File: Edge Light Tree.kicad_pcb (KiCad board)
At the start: 2 copper layers, 94 x 32 mm, 40 parts, among them M1 Motor_DC, Q1 2SC1815, Q2 2SC1815, Q3 2SC1815, Q4 2SC1815, Q5 2SC1815, Q6 2SC1815, SW1 SW_DIP_x01, SW2 SW_DIP_x01

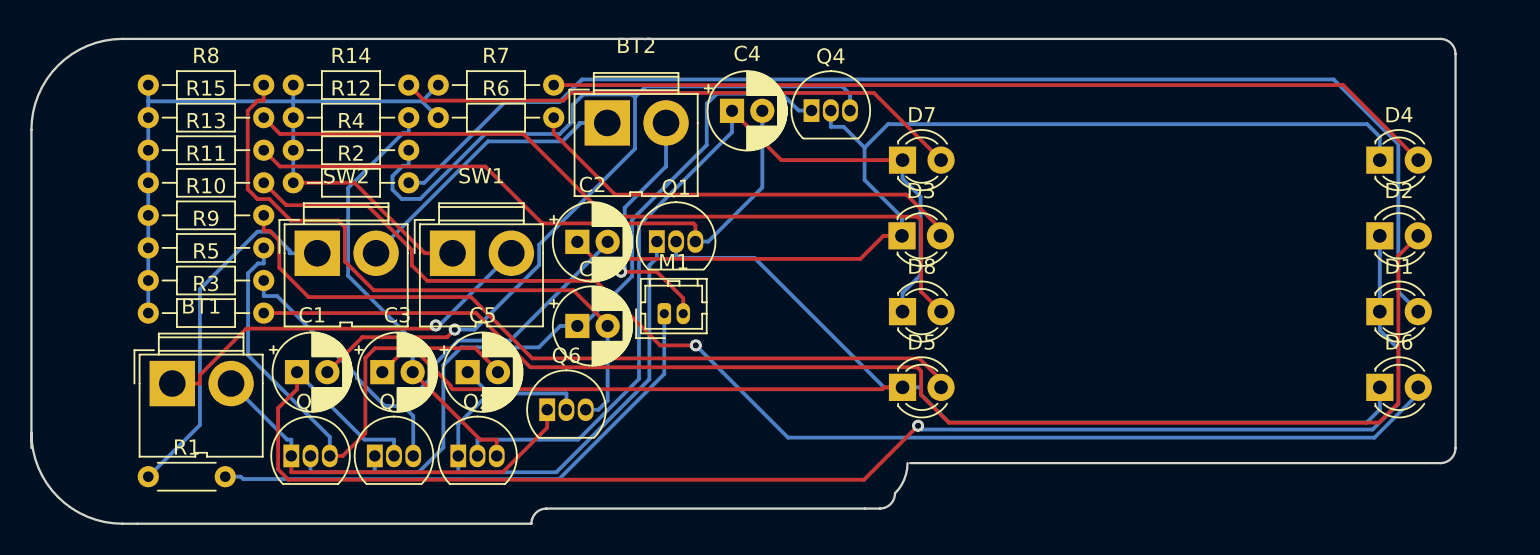
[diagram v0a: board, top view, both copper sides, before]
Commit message: Board mounting holes until installation
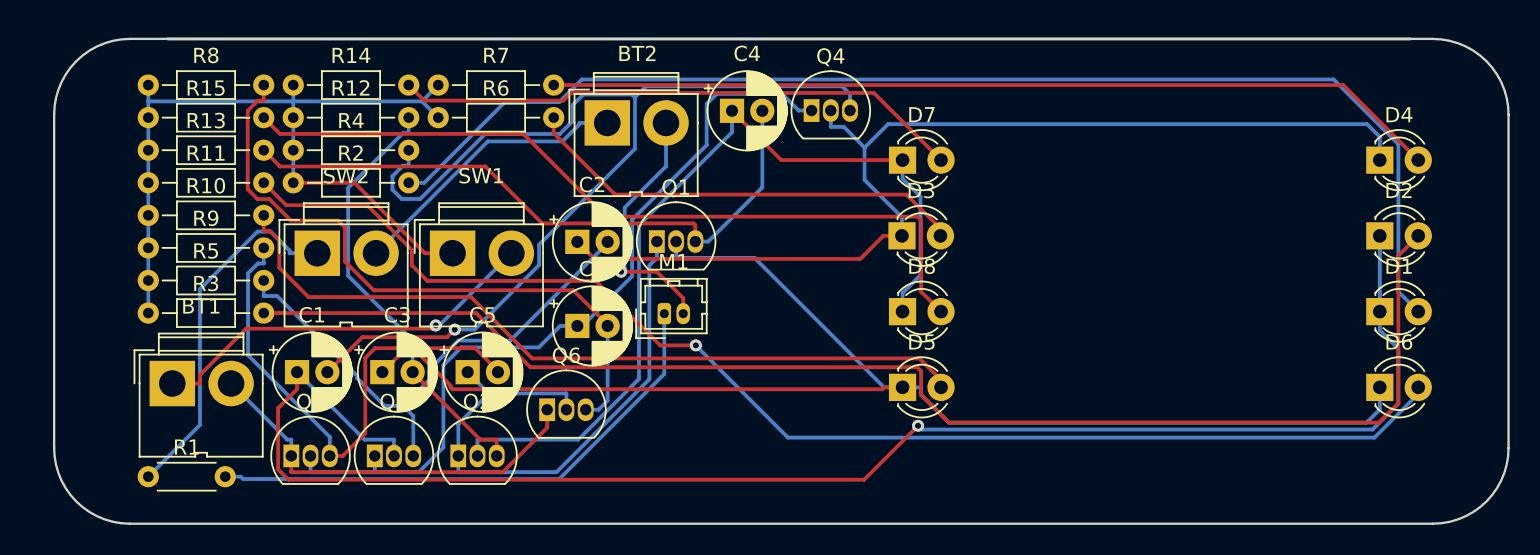
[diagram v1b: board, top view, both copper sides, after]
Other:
- board size 94 x 32 mm -> 96 x 32 mm
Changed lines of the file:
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@@
-(kicad_pcb (version 20171130) (host pcbnew "(5.0.2)-1")
+(kicad_pcb (version 20171130) (host pcbnew "(5.0.1-3-g963ef8bb5)")
   (general
     (thickness 1.6)
-    (drawings 17)
+    (drawings 15)
     (tracks 305)
     (zones 0)
@@
     (descr "JWT A3963, 3.96mm pitch Pin head connector (http://www.jwt.com.tw/pro_pdf/A3963.pdf)")
     (tags "connector JWT A3963 pinhead")
-    (fp_text reference BT2 (at 1.91 -5.08) (layer F.SilkS)
+    (fp_text reference BT2 (at 1.992 -4.5464) (layer F.SilkS)
       (effects (font (size 1 1) (thickness 0.15)))
     )
@@
     )
   )
-  (gr_line (start 110 80) (end 110 101) (layer Edge.Cuts) (width 0.15))
-  (gr_line (start 116 74) (end 117 74) (layer Edge.Cuts) (width 0.15))
-  (gr_arc (start 116 80) (end 116 74) (angle -90) (layer Edge.Cuts) (width 0.15))
-  (gr_arc (start 116 100) (end 110 100) (angle -90) (layer Edge.Cuts) (width 0.15))
-  (gr_line (start 117 106) (end 116 106) (layer Edge.Cuts) (width 0.15))
-  (gr_line (start 117 74) (end 203 74) (layer Edge.Cuts) (width 0.15))
-  (gr_arc (start 203 75) (end 204 75) (angle -90) (layer Edge.Cuts) (width 0.15))
-  (gr_line (start 204 101) (end 204 75) (layer Edge.Cuts) (width 0.15))
-  (gr_arc (start 203 101) (end 203 102) (angle -90) (layer Edge.Cuts) (width 0.15))
-  (gr_line (start 202 102) (end 203 102) (layer Edge.Cuts) (width 0.15))
-  (gr_line (start 168 102) (end 202 102) (layer Edge.Cuts) (width 0.15))
-  (gr_arc (start 165 102) (end 166.999999 103.999999) (angle -45) (layer Edge.Cuts) (width 0.15))
-  (gr_arc (start 166 104) (end 166 105) (angle -90) (layer Edge.Cuts) (width 0.15))
-  (gr_line (start 165 105) (end 166 105) (layer Edge.Cuts) (width 0.15))
-  (gr_line (start 144 105) (end 165 105) (layer Edge.Cuts) (width 0.15))
-  (gr_arc (start 144 106) (end 144 105) (angle -90) (layer Edge.Cuts) (width 0.15))
-  (gr_line (start 117 106) (end 143 106) (layer Edge.Cuts) (width 0.15))
+  (target plus (at 114.5 77.5) (size 5) (width 0.15) (layer Edge.Cuts))
+  (target plus (at 114.5 102) (size 5) (width 0.15) (layer Edge.Cuts))
+  (target plus (at 204 102) (size 5) (width 0.15) (layer Edge.Cuts))
+  (target plus (at 204 77.5) (size 5) (width 0.15) (layer Edge.Cuts))
+  (gr_line (start 116.5 106) (end 202.5 106) (layer Edge.Cuts) (width 0.15))
+  (gr_arc (start 202.5 101) (end 202.5 106) (angle -90) (layer Edge.Cuts) (width 0.15))
+  (gr_line (start 207.5 79) (end 207.5 101) (layer Edge.Cuts) (width 0.15))
+  (gr_line (start 111.5 79) (end 111.5 101) (layer Edge.Cuts) (width 0.15))
+  (gr_arc (start 116.5 101) (end 111.5 101) (angle -90) (layer Edge.Cuts) (width 0.15))
+  (gr_line (start 116.5 74) (end 119 74) (layer Edge.Cuts) (width 0.15))
+  (gr_arc (start 116.5 79) (end 116.5 74) (angle -90) (layer Edge.Cuts) (width 0.15))
+  (gr_line (start 202 74) (end 202.5 74) (layer Edge.Cuts) (width 0.15))
+  (gr_arc (start 202.5 79) (end 207.5 79) (angle -90) (layer Edge.Cuts) (width 0.15))
+  (gr_line (start 201 74) (end 202 74) (layer Edge.Cuts) (width 0.15))
+  (gr_line (start 119 74) (end 201 74) (layer Edge.Cuts) (width 0.2))
   (segment (start 127.153 101.526) (end 127.153 102.6013) (width 0.25) (layer F.Cu) (net 1))
   (segment (start 144.043 98.4764) (end 144.043 99.6642) (width 0.25) (layer F.Cu) (net 1))

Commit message: ほぼ完成版
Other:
- outline, holes or cut-outs redrawn
- board text added: "Shunnosuke Tokuhira"
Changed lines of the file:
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@@
   (general
     (thickness 1.6)
-    (drawings 15)
+    (drawings 20)
     (tracks 305)
     (zones 0)
@@
     (0 F.Cu mixed)
     (31 B.Cu mixed)
-    (32 B.Adhes user)
-    (33 F.Adhes user)
+    (32 B.Adhes user hide)
+    (33 F.Adhes user hide)
     (34 B.Paste user)
     (35 F.Paste user)
@@
     (43 Eco2.User user)
     (44 Edge.Cuts user)
-    (45 Margin user)
-    (46 B.CrtYd user)
+    (45 Margin user hide)
+    (46 B.CrtYd user hide)
     (47 F.CrtYd user)
-    (48 B.Fab user)
-    (49 F.Fab user)
+    (48 B.Fab user hide)
+    (49 F.Fab user hide)
   )
   (setup
@@
     (visible_elements 7FFFFFFF)
     (pcbplotparams
-      (layerselection 0x010fc_ffffffff)
+      (layerselection 0x090fc_ffffffff)
       (usegerberextensions false)
       (usegerberattributes false)
@@
       (outputformat 1)
       (mirror false)
-      (drillshape 1)
+      (drillshape 0)
       (scaleselection 1)
       (outputdirectory ""))
@@
     )
   )
+  (gr_text "Shunnosuke Tokuhira" (at 168.6941 103.22052) (layer F.CrtYd)
+    (effects (font (size 1.5 1.5) (thickness 0.3)) (justify left))
+  )
+  (gr_line (start 198 80) (end 171 80) (layer Edge.Cuts) (width 0.15))
+  (gr_line (start 198 99) (end 198 80) (layer Edge.Cuts) (width 0.15))
+  (gr_line (start 171 99) (end 198 99) (layer Edge.Cuts) (width 0.15))
+  (gr_line (start 171 80) (end 171 99) (layer Edge.Cuts) (width 0.15))
   (target plus (at 114.5 77.5) (size 5) (width 0.15) (layer Edge.Cuts))
   (target plus (at 114.5 102) (size 5) (width 0.15) (layer Edge.Cuts))
